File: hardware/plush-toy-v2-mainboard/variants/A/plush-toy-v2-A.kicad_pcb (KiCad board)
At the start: 4 copper layers, 52 x 46 mm, 98 parts, among them U1 ESP32-S3-WROOM-1-N16R8

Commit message: feat(pcb-v2): 喇叭座改为 SH1.0 2P，与测温、触摸统一
委托方要求接口规格尽量统一。重新布局布线，DRC 0 错误 0 未连接；
料号 38 种，扩展库 20 种。

Co-Authored-By: Claude Opus 5.5 <noreply@anthropic.com>
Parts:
- removed the J_SPK at (39.2, 42.4)
- added J_SPK: SH1.0-2P, Connector_JST:JST_SH_SM02B-SRSS-TB_1x02-1MP_P1.00mm_Horizontal, F.Cu at (39.2, 42.2)
- moved C_EFUSE_DVDT 21.1 mm to (41.0, 38.2)
- moved D_USB_DN 12.9 mm to (35.0, 43.2), turned to 90 degrees
- moved D_USB_DP 12.9 mm to (35.2, 41.2), turned to 0 degrees
- moved C_AMP_BULK 11.2 mm to (36.2, 38.0), turned to 0 degrees
- moved C_VBAT_SENSE 10.5 mm to (19.2, 43.2)
- moved R_EFUSE_ILM 9.65 mm to (27.8, 32.0), turned to 90 degrees
- moved C_NTC 8.50 mm to (43.2, 43.8)
- moved R_CC_SUM1 5.34 mm to (22.5, 44.5)
- moved R_CC2 5.27 mm to (22.5, 39.5), turned to 90 degrees
- moved R_BAT_NTC 3.26 mm to (21.5, 41.8), turned to 90 degrees
- moved R_CC1 2.75 mm to (22.8, 42.0)
- moved C_EFUSE_IN 1.58 mm to (41.0, 36.2), turned to 90 degrees
- moved C_CC_SENSE 1.25 mm to (21.2, 44.2), turned to 90 degrees
- moved C_AMP 0.56 mm to (43.2, 38.2)
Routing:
- net CC1: track 7.64 -> 28.0 mm, vias 0 -> 2
- net VSYS: track 73.4 -> 90.9 mm, vias 12 -> 17
- net KEY_MUTE: track 43.6 -> 28.7 mm
- net AMP_DIN: track 75.2 -> 60.7 mm
- net I2C_SDA: track 60.7 -> 46.8 mm, vias 4 -> 5
- net AMP_LRCLK: track 42.4 -> 55.5 mm
- net EFUSE_DVDT: track 12.5 -> 24.5 mm, vias 0 -> 2
- net HEAT_GATE_DRV: track 44.9 -> 56.4 mm
- net USB_DP: track 37.8 -> 28.0 mm, vias 0 -> 4
- net I2C_SCL: track 54.1 -> 44.7 mm, vias 4 -> 0
- net SPK_N: track 17.3 -> 8.85 mm, vias 0 -> 2
- net SERVO_L_PWM: track 56.9 -> 48.7 mm
- net CC_SENSE: track 45.1 -> 37.1 mm, vias 3 -> 4
- net LCD_BL_PWM: track 29.6 -> 21.8 mm, vias 2 -> 4
- net AMP_SD: track 19.3 -> 12.5 mm, vias 4 -> 2
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
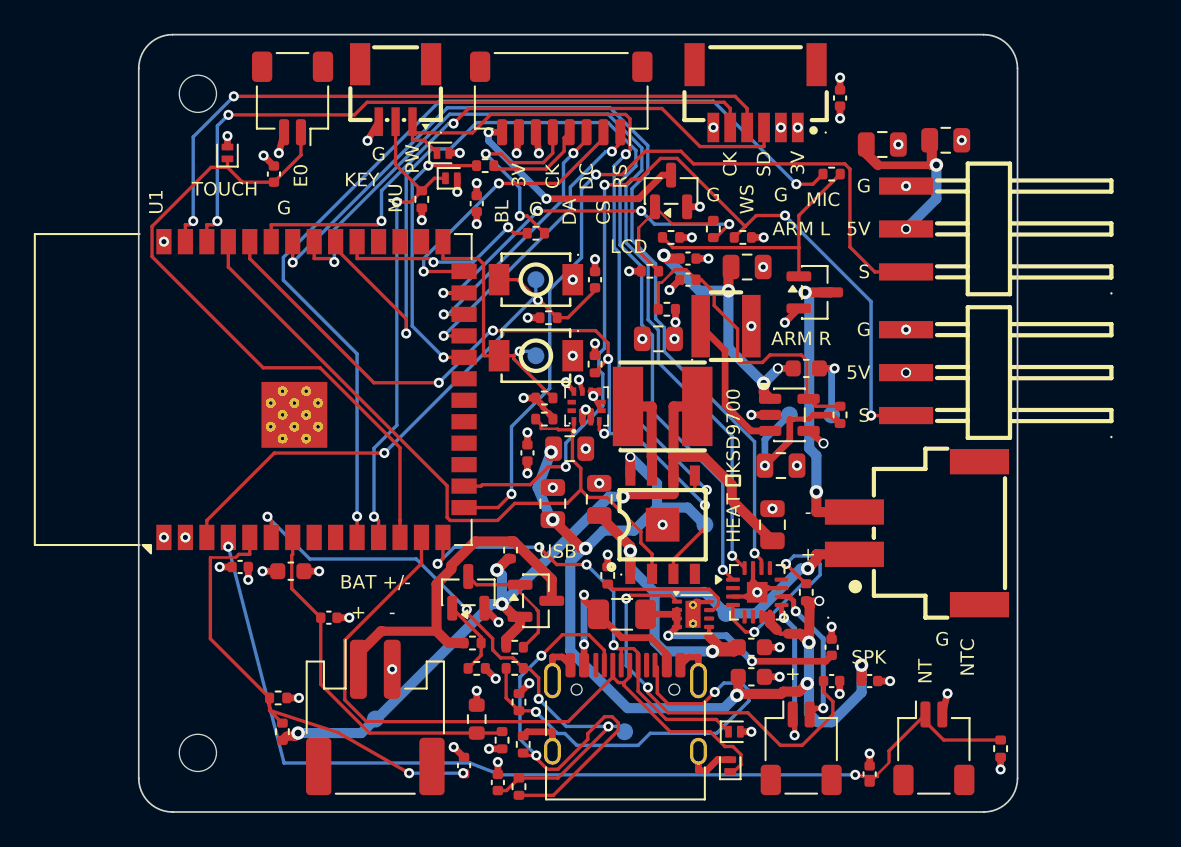
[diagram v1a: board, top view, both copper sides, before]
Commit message: fix(pcb-v2): 版本 A 去耦布局复查修正，板子加宽到 54×46
复查发现去耦电容只按「附近」放（降压高频电容离引脚 9.9mm、反馈网络 10mm），DRC 查不出。
- 去耦件按引脚就近、同侧放置并加测试（第一颗 ≤3mm，储能 ≤6mm，降压高频电容地焊盘也贴地脚）
- 放置顺序：去耦 → 引脚标注 → 储能电容 → 功能名（长的先排、不得印到邻座旁）→ 其余
- In2 改 VSYS L 形 + 3V3 整层低优先级：降压输出焊盘直接进 3V3 平面，VSYS 不再走细线
- 补线器检查孔距，hole_to_hole 按错误处理；降压热回路表层直连 1.2mm
- 电池座换国产 HX PH2.0-2PWT（C22461285），单板器件费约 $13.1
- 新测试：焊盘间距、功率网络细线、出线座卧式且开口朝板边、功能名归属
- 委托方同意加宽 2mm：54×46mm，一期面积的 46%；DRC 0 错误 0 未连接

Co-Authored-By: Claude Opus 5.5 <noreply@anthropic.com>
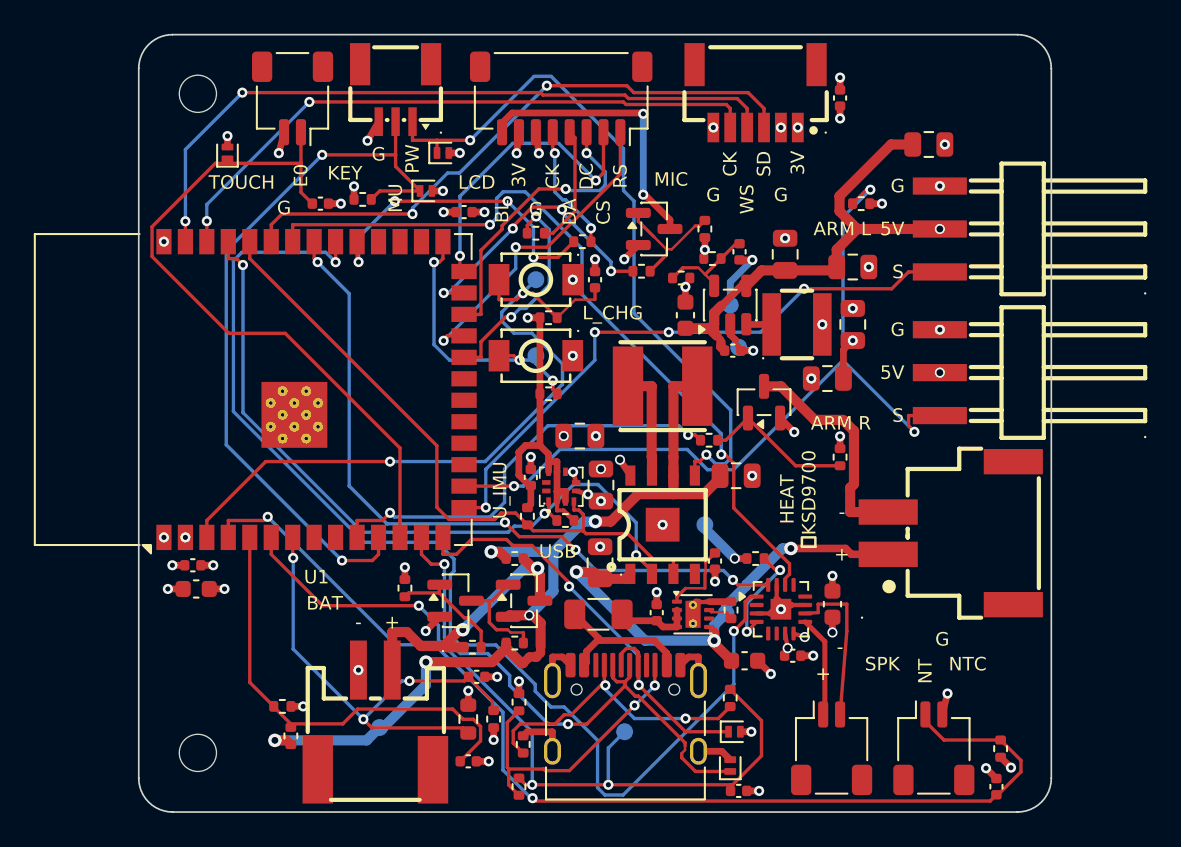
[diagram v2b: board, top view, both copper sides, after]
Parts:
- removed the J_BAT at (14.0, 40.4)
- added J_BAT: BAT PH2.0, plushv2:CONN-SMD_2P-P2.00_HANXIA_HX-PH2.0-2PWT, F.Cu at (14.0, 40.5)
- moved R_GATE 17.3 mm to (33.8, 24.0)
- moved R_GATE_PD 16.4 mm to (41.5, 25.0), turned to 90 degrees
- moved C_CC_SENSE 14.3 mm to (35.5, 44.8), turned to 0 degrees
- moved R_CC_SUM1 13.6 mm to (35.0, 39.2)
- moved C_SERVO1 13.0 mm to (46.8, 6.50)
- moved R_FB1 11.9 mm to (34.0, 13.2), turned to 0 degrees
- moved C_SERVO3 11.7 mm to (38.2, 13.0), turned to 90 degrees
- moved C_EFUSE_IN 10.6 mm to (30.6, 34.2)
- moved C_BUCK_OUT2 10.3 mm to (40.8, 20.4), turned to 180 degrees
- moved C_EFUSE_DVDT 9.90 mm to (34.1, 31.1), turned to -90 degrees
- moved R_SDA 9.85 mm to (23.0, 28.5)
- moved C_BAT_NTC 9.42 mm to (20.0, 38.0)
- moved C_BUCK_OUT1 9.37 mm to (42.2, 17.1), turned to 90 degrees
- moved C_BUCK_IN 7.81 mm to (32.4, 16.6), turned to 90 degrees
- moved R_EFUSE_ILM 7.58 mm to (35.0, 34.0)
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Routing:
- net VSYS: track 90.9 -> 35.3 mm, vias 17 -> 9
- net HEAT_GATE_DRV: track 56.4 -> 25.4 mm
- net EFUSE_DVDT: track 24.5 -> 4.48 mm, vias 2 -> 0
- net KEY_MUTE: track 28.7 -> 44.7 mm
- net BUCK_FB: track 19.1 -> 6.02 mm
- net SERVO_L_PWM: track 48.7 -> 36.2 mm, vias 2 -> 4
- net AMP_BCLK: track 54.2 -> 42.6 mm, vias 2 -> 4
- net CC_SENSE: track 37.1 -> 48.3 mm, vias 4 -> 3
- net CC1: track 28.0 -> 18.0 mm
- net CC2: track 27.1 -> 17.6 mm
- net VBUS_FUSED: track 14.0 -> 4.56 mm, vias 2 -> 0
- net AMP_LRCLK: track 55.5 -> 46.2 mm
- net USB_DN: track 41.8 -> 33.1 mm, vias 0 -> 2
- net EN: track 34.8 -> 43.4 mm
- net AMP_DIN: track 60.7 -> 69.1 mm
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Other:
- board size 52 x 46 mm -> 54 x 46 mm
- board text added: "BAT"
- board text removed: "BAT +/-"
